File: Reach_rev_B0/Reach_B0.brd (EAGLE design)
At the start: 107.3 x 69.5 mm, 92 parts, among them IC1 TMC2100-LA, IC18 74AHC1G126DCK, IC2 TMC2100-LA, IC3 74AHC1G126DCK, IC4 74AHC1G126DCK, IC8 74AHC1G126DCK, IC9 74AHC1G126DCK, P8 F-2X23-, P9 F-2X23-, Q2 AON6758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

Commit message: Updated readmen
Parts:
- moved C41 4.84 mm to (30.3, 41.7)
- moved C5 1.97 mm to (33.2, 43.5)
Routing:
- net +3V3: track 491.3 -> 6.16 mm, vias 23 -> 0
- net FAN5: track 162.6 -> 0.00 mm, vias 4 -> 0
- net FAN6: track 137.8 -> 0.00 mm, vias 4 -> 0
- net FAN4: track 135.9 -> 0.00 mm, vias 4 -> 0
- net FAN7: track 121.6 -> 0.00 mm, vias 4 -> 0
- net FAULT_Y: track 120.3 -> 0.00 mm, vias 4 -> 0
- net SPI1_CS0: track 113.9 -> 0.00 mm, vias 6 -> 0
- net ENABLE_XYZ: track 112.2 -> 0.00 mm, vias 5 -> 0
- net SPI1_SCLK: track 104.5 -> 0.00 mm, vias 6 -> 0
- net TRISTATE_STEPPERS: track 64.4 -> 0.00 mm, vias 3 -> 0
- net SERVO_0_EN: track 59.6 -> 0.00 mm, vias 2 -> 0
- net SPI1_MOSI: track 52.4 -> 0.00 mm, vias 2 -> 0
- net HEATER_A: track 52.1 -> 4.70 mm, vias 4 -> 0
- net IREF_Y_RAW: track 46.7 -> 0.00 mm, vias 2 -> 0
- net VDD_5V: track 62.4 -> 18.5 mm, vias 3 -> 0
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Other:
- board text removed: "0"
- board text removed: "1"
- board text removed: "2"
- board text removed: "3"
- board text removed: "Fans"
- board text removed: "X"
- board text removed: "Y"
- board text removed: "Z"

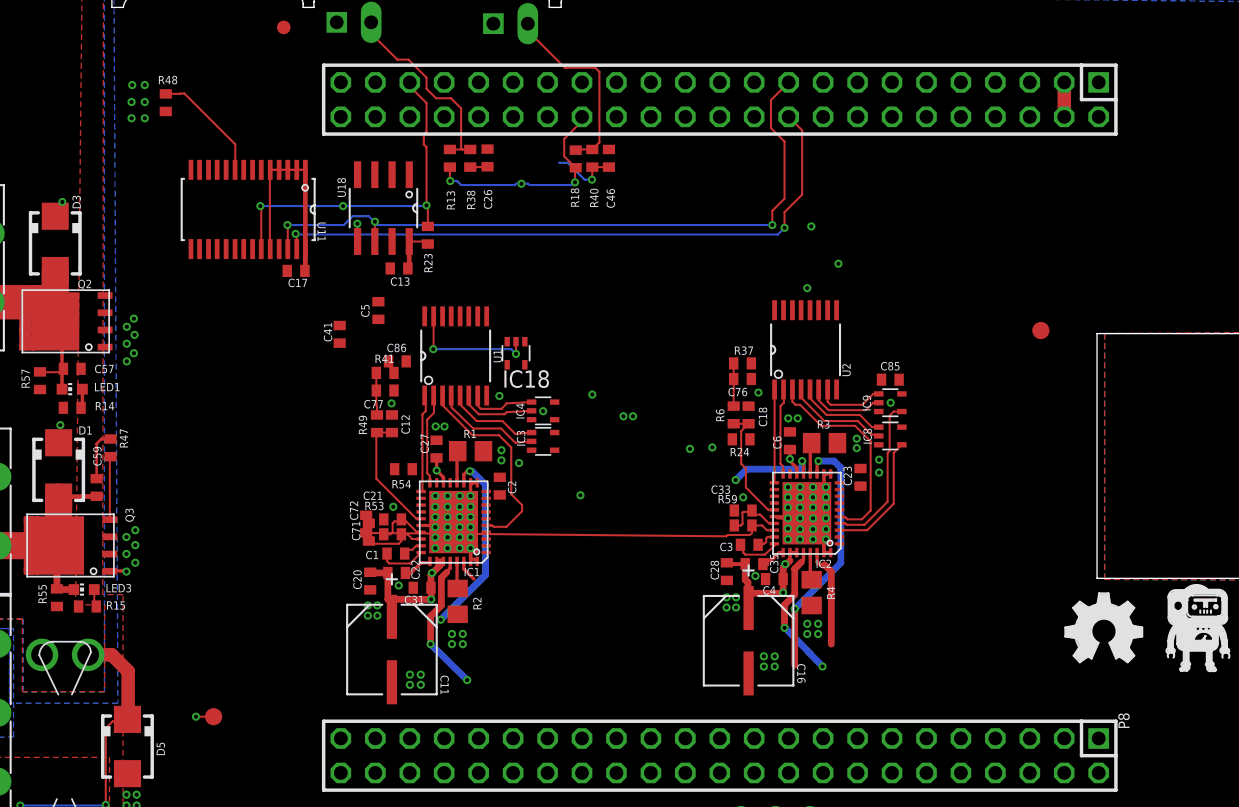
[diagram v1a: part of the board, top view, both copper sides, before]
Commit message: Added new version eeprom data
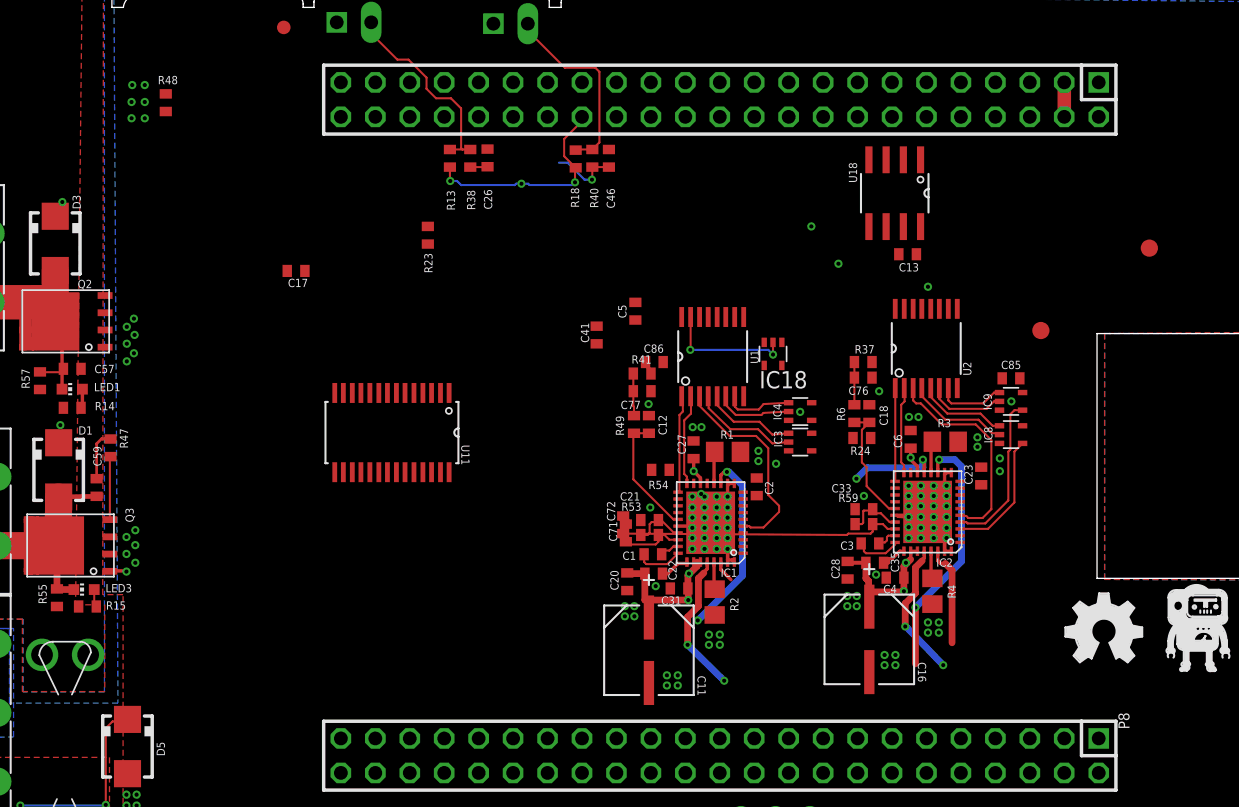
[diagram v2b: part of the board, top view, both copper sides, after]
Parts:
- moved 12..24V 77.2 mm to (90.0, 48.0)
- moved U18 37.7 mm to (71.3, 52.1)
- moved C13 37.5 mm to (72.2, 47.6)
- moved U11 19.6 mm to (34.2, 34.5)
- moved C1 19.0 mm to (53.4, 25.5)
- moved C2 19.0 mm to (61.1, 30.4)
- moved C21 19.0 mm to (53.2, 28.0)
- moved C22 19.0 mm to (53.5, 24.1)
- moved C27 19.0 mm to (56.4, 33.2)
- moved C71 19.0 mm to (51.5, 27.1)
- moved C72 19.0 mm to (51.2, 27.6)
- moved IC1 19.0 mm to (57.7, 27.8)
- moved R1 19.0 mm to (59.0, 33.0)
- moved R2 19.0 mm to (58.0, 21.9)
- moved R53 19.0 mm to (53.2, 26.9)
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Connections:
- new net THERMO_1: P9.37
- new net THERMO_2: P9.38
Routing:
- net I2C2_SCL: track 51.5 -> 0.00 mm, vias 3 -> 0
- net I2C2_SDA: track 48.7 -> 0.00 mm, vias 3 -> 0
- net ENABLE: track 26.9 -> 0.00 mm, vias 3 -> 0
- net VDD_5V: track 18.5 -> 0.00 mm
- net N$110: track 30.9 -> 20.8 mm
- net HEATER_B: track 8.68 -> 0.11 mm
- net VDD_IN: track 55.9 -> 47.6 mm, vias 11 -> 10
- net +3V3: track 6.16 -> 2.70 mm
- net GND: vias 123 -> 117
- removed copper zone on layer 3, net VDD_12V
- removed copper zone on layer 3, net VDD_5V

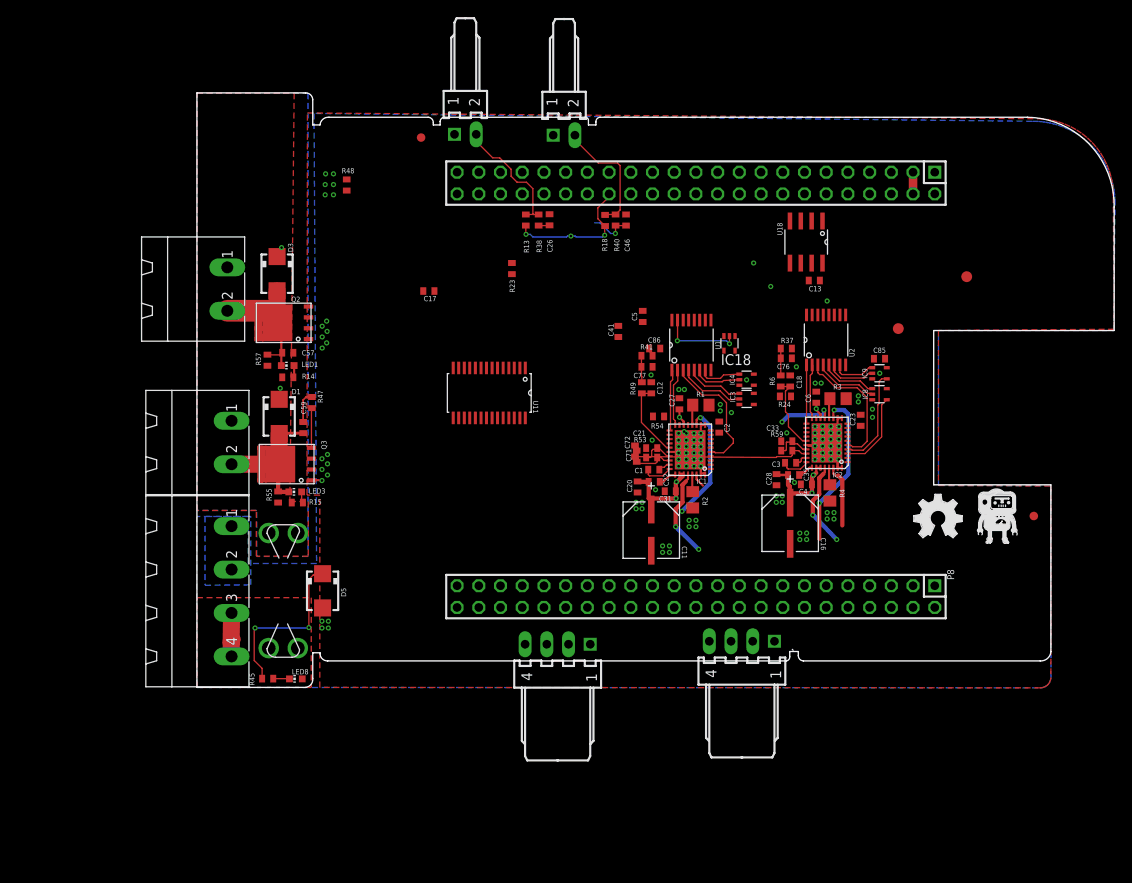
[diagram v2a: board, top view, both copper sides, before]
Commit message: Added a Collada (DAE) file
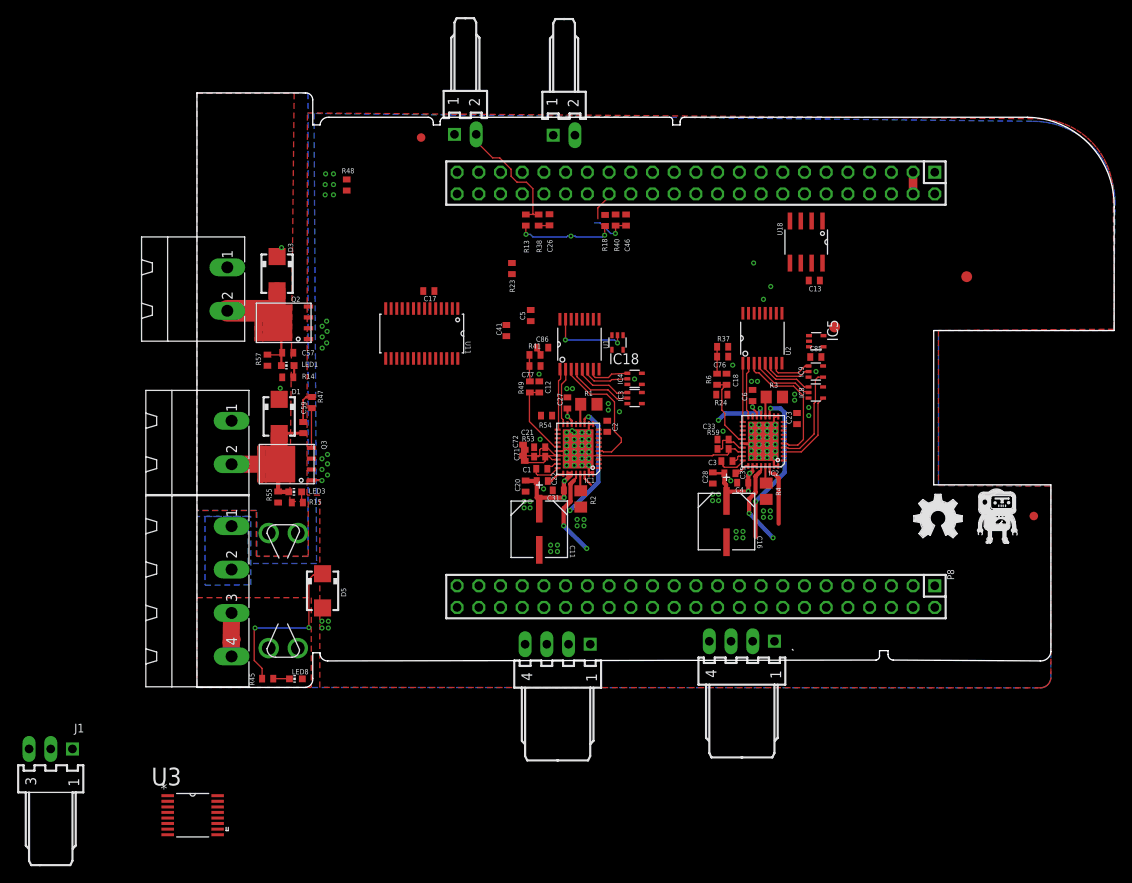
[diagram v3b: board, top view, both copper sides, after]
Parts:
- added IC5: 74AHC1G126DCK, 74xx-little-de:SC70-5
- added J1: 22-05-7038-03, con-molex:7395-03
- added U3: TS3A5018PW, Texas Instruments_By_element14_Batch_1:SOP65P640X120-16N
- moved C1 13.1 mm to (40.3, 25.6)
- moved C11 13.1 mm to (40.0, 18.5)
- moved C12 13.1 mm to (40.0, 35.1)
- moved C2 13.1 mm to (48.0, 30.6)
- moved C21 13.1 mm to (40.1, 28.1)
- moved C22 13.1 mm to (40.4, 24.1)
- moved C27 13.1 mm to (43.3, 33.3)
- moved C31 13.1 mm to (42.3, 23.1)
- moved C5 13.1 mm to (39.0, 43.5)
- moved C71 13.1 mm to (38.4, 27.1)
- moved C72 13.1 mm to (38.1, 27.8)
- moved C77 13.1 mm to (39.5, 37.6)
- moved IC1 13.1 mm to (44.6, 27.9)
- moved R1 13.1 mm to (45.9, 33.1)
- moved R2 13.1 mm to (44.9, 22.1)
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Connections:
- removed net ENABLE_XYZ: IC1.22, IC18.4, IC2.22
- removed net SERVO_0_EN: U2.15
- new net ENABLE_A: IC1.22, IC18.4
- new net ENABLE_B: IC2.22, IC5.4
- new net N$1: IC5.2, U2.15
- new net N$11: C26.2, X8.1
- new net N$9: C46.2
- new net V+: U3.16
- new net VCC: IC5.5
- net GND: now also IC5.3; no longer C26.2, C46.2, X8.1
- net N$240: no longer R18.1, R40.1
- net VDD_ADC: no longer R18.2
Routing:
- net N$240: track 14.2 -> 0.00 mm
- net N$110: track 20.8 -> 26.5 mm
- net VDD_ADC: track 16.3 -> 15.0 mm
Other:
- outline, holes or cut-outs redrawn
- board text removed: "12V"
- board text removed: "X1"
- board text removed: "X2"
- board text removed: "Y1"
- board text removed: "Y2"
- board text removed: "Z1"
- board text removed: "Z2"
